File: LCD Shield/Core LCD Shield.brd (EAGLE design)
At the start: 38.1 x 35.6 mm, 8 parts, among them IC1 MC33269T-5.0, J1 TWIG_2.0-DIP-FEMALE

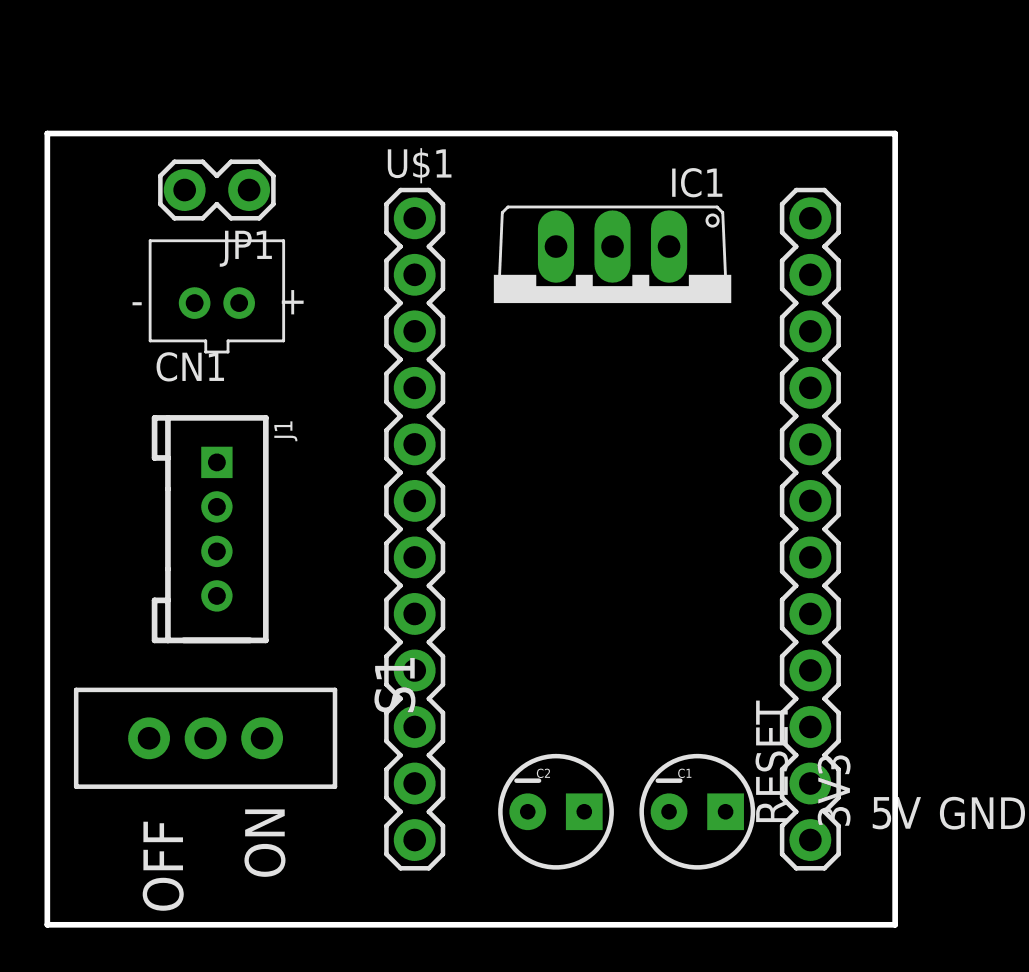
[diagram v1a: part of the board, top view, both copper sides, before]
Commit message: Made a few more changes to the LCD shield
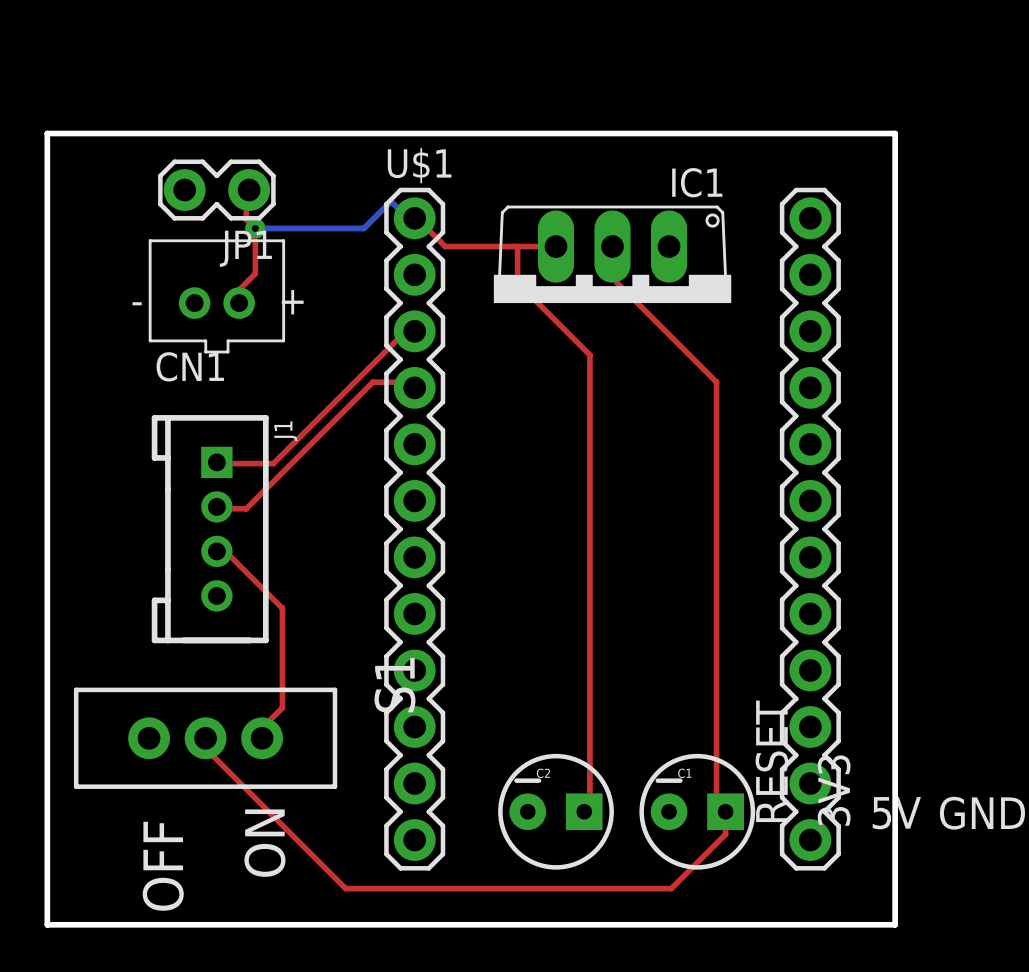
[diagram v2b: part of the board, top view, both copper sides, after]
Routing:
- net N1: track 0.00 -> 56.1 mm
- net VIN: track 0.00 -> 47.4 mm, vias 0 -> 1
- net TX: track 0.00 -> 11.5 mm
- net RX: track 0.00 -> 11.4 mm
- net +5V: track 0.00 -> 10.5 mm
- added copper zone on layer 1, net GND
- added copper zone on layer 16, net GND
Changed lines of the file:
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@@
 <contactref element="S1" pad="1"/>
 <contactref element="J1" pad="3"/>
-<wire x1="9.652" y1="8.382" x2="7.62" y2="16.78" width="0" layer="19" extent="1-1"/>
+<wire x1="8.128" y1="16.6624" x2="7.7216" y2="16.6624" width="0.254" layer="1"/>
+<wire x1="10.5664" y1="14.224" x2="8.128" y2="16.6624" width="0.254" layer="1"/>
+<wire x1="10.5664" y1="9.7536" x2="10.5664" y2="14.224" width="0.254" layer="1"/>
+<wire x1="9.3472" y1="8.5344" x2="10.5664" y2="9.7536" width="0.254" layer="1"/>
+<wire x1="7.7216" y1="16.6624" x2="7.62" y2="16.78" width="0.254" layer="1"/>
+<wire x1="9.3472" y1="8.5344" x2="9.652" y2="8.382" width="0.254" layer="1"/>
 </signal>
 <signal name="GND">
@@
 <contactref element="JP1" pad="2"/>
 <contactref element="J1" pad="4"/>
-<wire x1="34.29" y1="24.13" x2="27.94" y2="30.48" width="0" layer="19" extent="1-1"/>
-<wire x1="16.51" y1="29.21" x2="27.94" y2="30.48" width="0" layer="19" extent="1-1"/>
-<wire x1="6.62" y1="27.94" x2="16.51" y2="29.21" width="0" layer="19" extent="1-1"/>
-<wire x1="6.1722" y1="33.02" x2="6.62" y2="27.94" width="0" layer="19" extent="1-1"/>
-<wire x1="7.62" y1="14.78" x2="6.62" y2="27.94" width="0" layer="19" extent="1-1"/>
-<wire x1="21.59" y1="5.08" x2="7.62" y2="14.78" width="0" layer="19" extent="1-1"/>
-<wire x1="27.94" y1="5.08" x2="21.59" y2="5.08" width="0" layer="19" extent="1-1"/>
+<polygon width="0.254" layer="16">
+<vertex x="0" y="0"/>
+<vertex x="0" y="35.56"/>
+<vertex x="38.1" y="35.56"/>
+<vertex x="38.1" y="0"/>
+</polygon>
+<polygon width="0.254" layer="1">
+<vertex x="0" y="0"/>
+<vertex x="0" y="35.56"/>
+<vertex x="38.1" y="35.56"/>
+<vertex x="38.1" y="0"/>
+</polygon>
 </signal>
 <signal name="RESET">
@@
 <contactref element="CN1" pad="1"/>
 <contactref element="JP1" pad="1"/>
-<wire x1="16.51" y1="31.75" x2="22.86" y2="30.48" width="0" layer="19" extent="1-1"/>
-<wire x1="9.0678" y1="33.02" x2="16.51" y2="31.75" width="0" layer="19" extent="1-1"/>
-<wire x1="8.62" y1="27.94" x2="9.0678" y2="33.02" width="0" layer="19" extent="1-1"/>
-<wire x1="24.13" y1="5.08" x2="22.86" y2="30.48" width="0" layer="19" extent="1-1"/>
+<wire x1="8.5344" y1="28.448" x2="8.5344" y2="28.0416" width="0.254" layer="1"/>
+<wire x1="9.3472" y1="29.2608" x2="8.5344" y2="28.448" width="0.254" layer="1"/>
+<wire x1="9.3472" y1="31.2928" x2="9.3472" y2="29.2608" width="0.254" layer="1"/>
+<wire x1="8.9408" y1="31.6992" x2="9.3472" y2="31.2928" width="0.254" layer="1"/>
+<wire x1="8.9408" y1="32.9184" x2="8.9408" y2="31.6992" width="0.254" layer="1"/>
+<wire x1="8.5344" y1="28.0416" x2="8.62" y2="27.94" width="0.254" layer="1"/>
+<wire x1="8.9408" y1="32.9184" x2="9.0678" y2="33.02" width="0.254" layer="1"/>
+<wire x1="17.8816" y1="30.48" x2="21.1328" y2="30.48" width="0.254" layer="1"/>
+<wire x1="21.1328" y1="30.48" x2="22.86" y2="30.48" width="0.254" layer="1"/>
+<wire x1="16.6624" y1="31.6992" x2="17.8816" y2="30.48" width="0.254" layer="1"/>
+<wire x1="16.6624" y1="31.6992" x2="16.51" y2="31.75" width="0.254" layer="1"/>
+<wire x1="24.384" y1="25.6032" x2="24.384" y2="5.2832" width="0.254" layer="1"/>
+<wire x1="21.1328" y1="28.8544" x2="24.384" y2="25.6032" width="0.254" layer="1"/>
+<wire x1="21.1328" y1="30.48" x2="21.1328" y2="28.8544" width="0.254" layer="1"/>
+<wire x1="24.384" y1="5.2832" x2="24.13" y2="5.08" width="0.254" layer="1"/>
+<wire x1="14.224" y1="31.2928" x2="9.3472" y2="31.2928" width="0.254" layer="16"/>
+<wire x1="15.4432" y1="32.512" x2="14.224" y2="31.2928" width="0.254" layer="16"/>
+<wire x1="16.256" y1="31.6992" x2="15.4432" y2="32.512" width="0.254" layer="16"/>
+<wire x1="16.256" y1="31.6992" x2="16.51" y2="31.75" width="0.254" layer="16"/>
+<via x="9.3472" y="31.2928" extent="1-16" drill="0.3048"/>
 </signal>
 <signal name="+3V3">
@@
 <contactref element="C1" pad="1"/>
 <contactref element="S1" pad="2"/>
-<wire x1="30.48" y1="5.08" x2="25.4" y2="30.48" width="0" layer="19" extent="1-1"/>
-<wire x1="7.112" y1="8.382" x2="30.48" y2="5.08" width="0" layer="19" extent="1-1"/>
+<wire x1="25.6032" y1="28.8544" x2="25.6032" y2="30.48" width="0.254" layer="1"/>
+<wire x1="30.0736" y1="24.384" x2="25.6032" y2="28.8544" width="0.254" layer="1"/>
+<wire x1="30.0736" y1="5.6896" x2="30.0736" y2="24.384" width="0.254" layer="1"/>
+<wire x1="30.48" y1="5.2832" x2="30.0736" y2="5.6896" width="0.254" layer="1"/>
+<wire x1="25.6032" y1="30.48" x2="25.4" y2="30.48" width="0.254" layer="1"/>
+<wire x1="30.48" y1="5.2832" x2="30.48" y2="5.08" width="0.254" layer="1"/>
+<wire x1="7.3152" y1="7.7216" x2="7.3152" y2="8.128" width="0.254" layer="1"/>
+<wire x1="13.4112" y1="1.6256" x2="7.3152" y2="7.7216" width="0.254" layer="1"/>
+<wire x1="28.0416" y1="1.6256" x2="13.4112" y2="1.6256" width="0.254" layer="1"/>
+<wire x1="30.48" y1="4.064" x2="28.0416" y2="1.6256" width="0.254" layer="1"/>
+<wire x1="30.48" y1="5.08" x2="30.48" y2="4.064" width="0.254" layer="1"/>
+<wire x1="7.3152" y1="8.128" x2="7.112" y2="8.382" width="0.254" layer="1"/>
 </signal>
 <signal name="VDDA">
@@
 <contactref element="J1" pad="2"/>
 <contactref element="U$1" pad="4"/>
-<wire x1="7.62" y1="18.78" x2="16.51" y2="24.13" width="0" layer="19" extent="1-1"/>
+<wire x1="8.9408" y1="18.6944" x2="7.7216" y2="18.6944" width="0.254" layer="1"/>
+<wire x1="14.6304" y1="24.384" x2="8.9408" y2="18.6944" width="0.254" layer="1"/>
+<wire x1="16.256" y1="24.384" x2="14.6304" y2="24.384" width="0.254" layer="1"/>
+<wire x1="7.7216" y1="18.6944" x2="7.62" y2="18.78" width="0.254" layer="1"/>
+<wire x1="16.256" y1="24.384" x2="16.51" y2="24.13" width="0.254" layer="1"/>
 </signal>
 <signal name="TX">
 <contactref element="J1" pad="1"/>
 <contactref element="U$1" pad="3"/>
-<wire x1="7.62" y1="20.78" x2="16.51" y2="26.67" width="0" layer="19" extent="1-1"/>
+<wire x1="10.16" y1="20.7264" x2="7.7216" y2="20.7264" width="0.254" layer="1"/>
+<wire x1="16.256" y1="26.8224" x2="10.16" y2="20.7264" width="0.254" layer="1"/>
+<wire x1="7.7216" y1="20.7264" x2="7.62" y2="20.78" width="0.254" layer="1"/>
+<wire x1="16.256" y1="26.8224" x2="16.51" y2="26.67" width="0.254" layer="1"/>
 </signal>
 </signals>
